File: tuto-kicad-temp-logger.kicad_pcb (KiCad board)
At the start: 4 copper layers, 60 x 45 mm, 68 parts, among them J201 HOOYA_USB_306F, J202 Conn_01x01_Pin, J401 SHOU HAN TF-CARD H1.8, Q301 L8050QLT1G, Q302 L8050QLT1G, SW301 TE_FSM4JSMATR, SW302 TE_FSM4JSMATR, U201 SGM2212-3.3XKC3G, U202 CP2102N-Axx-xQFN28, U301 ESP32-C3-WROOM-02, U401 TMP102xxDRL

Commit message: Routage
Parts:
- moved TP203 16.4 mm to (121.3, 99.1)
- moved TP204 12.1 mm to (120.5, 105.0)
- moved TP406 12.1 mm to (157.7, 91.5)
- moved TP205 9.83 mm to (134.3, 112.9)
- moved R402 7.32 mm to (126.2, 95.4), turned to 180 degrees
- moved TP401 7.24 mm to (123.0, 93.0)
- moved TP402 7.02 mm to (128.3, 91.2)
- moved TP403 5.50 mm to (133.1, 89.2)
- moved TP206 5.30 mm to (135.6, 106.8)
- moved TP301 5.00 mm to (111.9, 109.6)
- moved D201 4.80 mm to (156.5, 106.7)
- moved R403 4.50 mm to (144.8, 87.5), turned to -90 degrees
- moved TP303 4.24 mm to (109.0, 92.5)
- moved TP404 3.97 mm to (137.8, 86.8)
- moved TP407 2.91 mm to (149.3, 82.5)
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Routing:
- net /MCU/I2C.SDA: track 0.00 -> 65.8 mm, vias 0 -> 1
- net /MCU/I2C.SCL: track 0.00 -> 54.6 mm, vias 0 -> 1
- net GND: track 0.00 -> 54.6 mm, vias 0 -> 51
- net /MCU/SD.CD: track 0.00 -> 49.6 mm, vias 0 -> 1
- net /MCU/SD.SCK: track 0.00 -> 45.1 mm, vias 0 -> 1
- net /MCU/SD.MISO: track 0.00 -> 43.2 mm, vias 0 -> 1
- net /MCU/SD.CS: track 0.00 -> 38.8 mm, vias 0 -> 2
- net /MCU/SD.MOSI: track 0.00 -> 38.7 mm, vias 0 -> 1
- net /MCU/GPIO9: track 0.00 -> 37.1 mm, vias 0 -> 3
- net /MCU/UART.ESP32_TX: track 0.00 -> 35.3 mm, vias 0 -> 2
- net /MCU/UART.ESP32_RX: track 0.00 -> 33.8 mm, vias 0 -> 2
- net /MCU/CHIP_PU: track 0.00 -> 31.4 mm, vias 0 -> 1
- net VBUS: track 0.00 -> 26.8 mm, vias 0 -> 5
- net /MCU/RTS: track 0.00 -> 24.5 mm, vias 0 -> 4
- net +3V3: track 0.00 -> 22.6 mm, vias 0 -> 17
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- added copper zone on F.Cu, net +3V3
- added copper zone on In2.Cu, net +3V3
- added copper zone on In1.Cu, net GND
- added copper zone on In2.Cu, net VBUS
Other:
- board text added: "+3V3"
- board text added: "CD"
- board text added: "CHIP_PU"
- board text added: "CS"
- board text added: "DTR"
- board text added: "ESP32_RX"
- board text added: "ESP32_TX"
- board text added: "GND"
- board text added: "GPIO10"
- board text added: "GPIO18"
- board text added: "GPIO19"
- board text added: "GPIO9"
- board text added: "MISO"
- board text added: "MOSI"
- board text added: "RTS"
- board text added: "SCK"
- board text added: "SCL"
- board text added: "SDA"
- board text added: "VBUS"

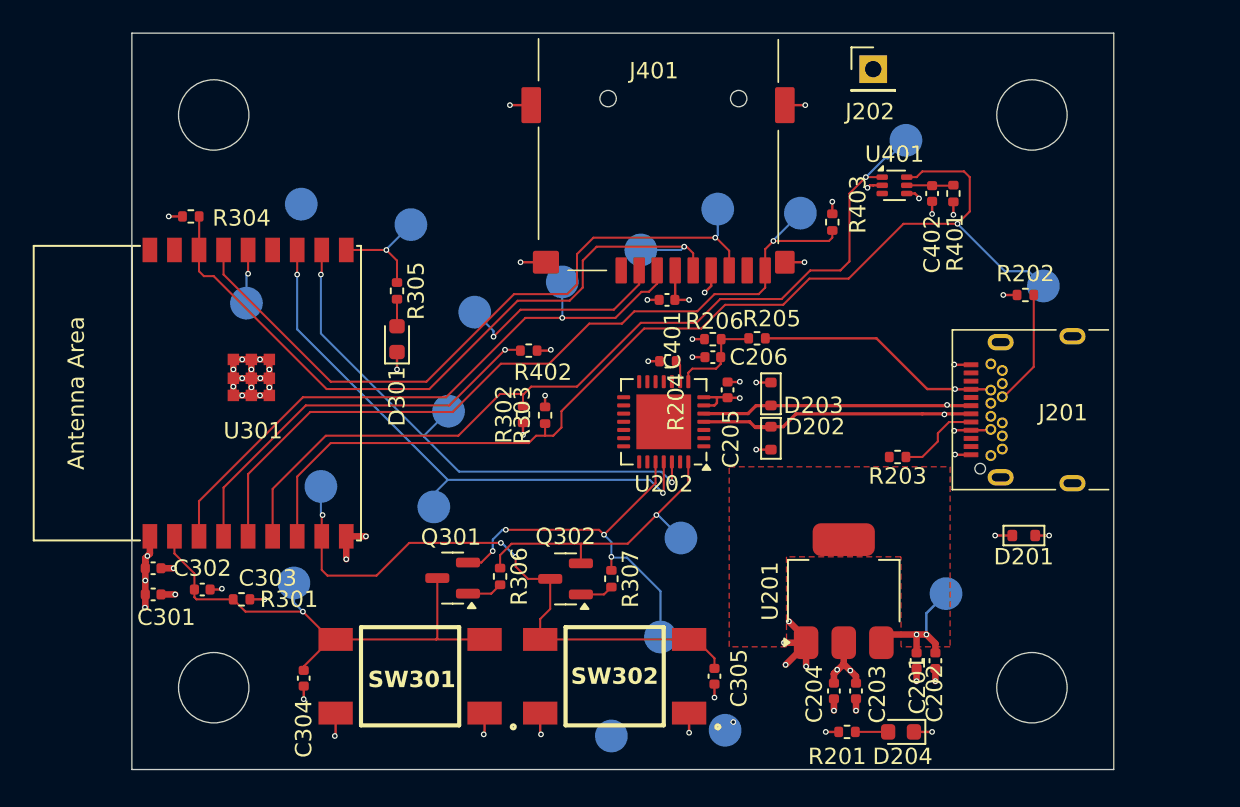
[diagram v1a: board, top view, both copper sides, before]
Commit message: Ajout de plans hachurés au top et bottom
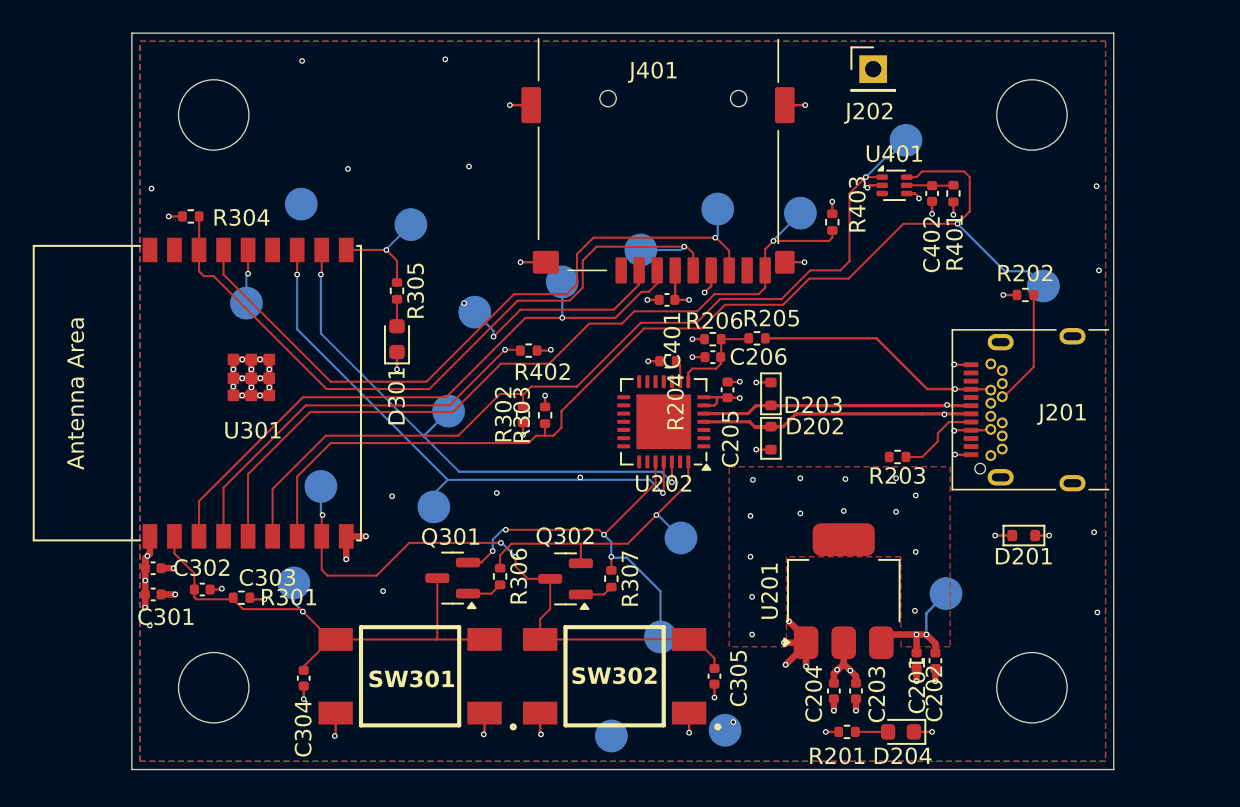
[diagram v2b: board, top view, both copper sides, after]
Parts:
- moved R301 0.10 mm to (108.7, 110.5)
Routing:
- net +3V3: track 22.6 -> 26.3 mm, vias 17 -> 31
- net GND: vias 51 -> 64
- net /MCU/UART.ESP32_TX: vias 2 -> 3
- net /MCU/SD.CS: vias 2 -> 3
- added copper zone on B.Cu, net GND
- added copper zone on F.Cu, net GND

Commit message: Ajout des annotations
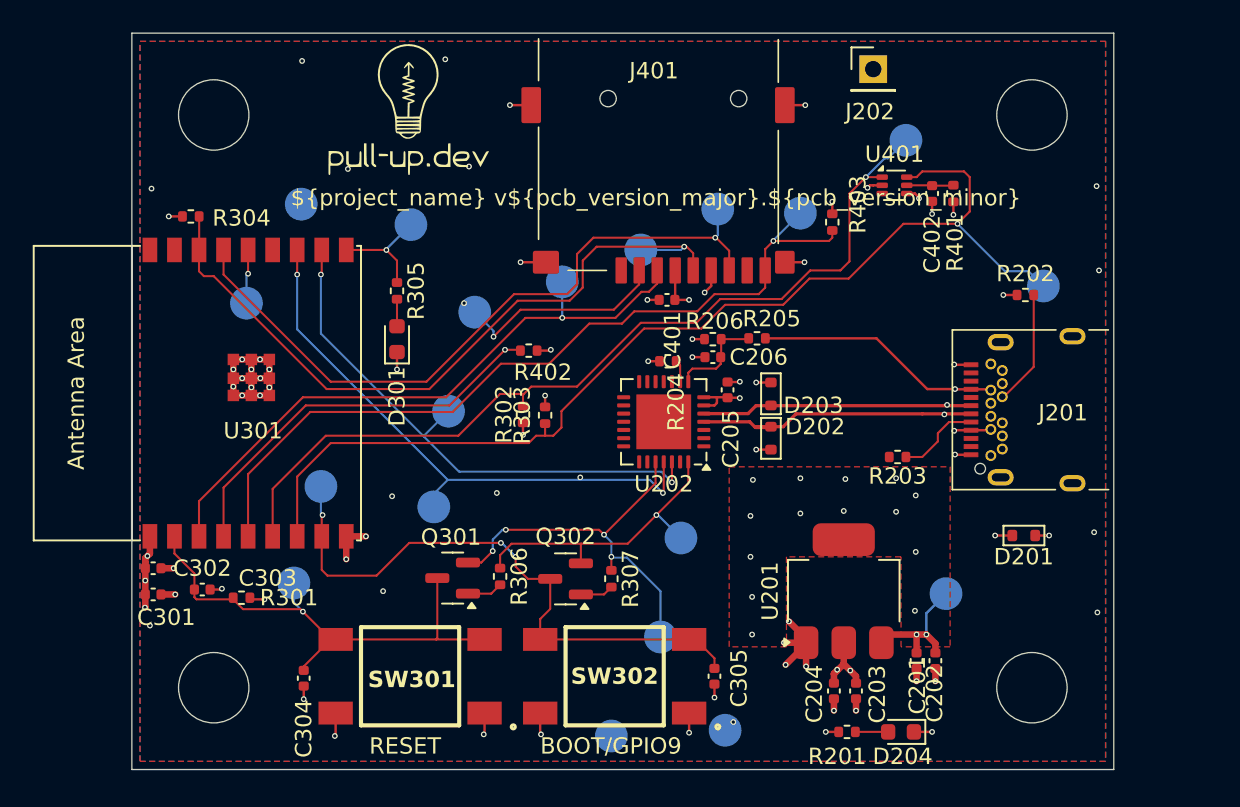
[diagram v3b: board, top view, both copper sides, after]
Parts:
- added G***: LOGO, tuto-kicad-temp-logger:logo, F.Cu at (118.9, 80.7)
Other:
- board text added: "${project_name} v${pcb_version_major}.${pcb_version_minor}"
- board text added: "BOOT/GPIO9"
- board text added: "RESET"

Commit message: Silkscreen, DRC et corrections
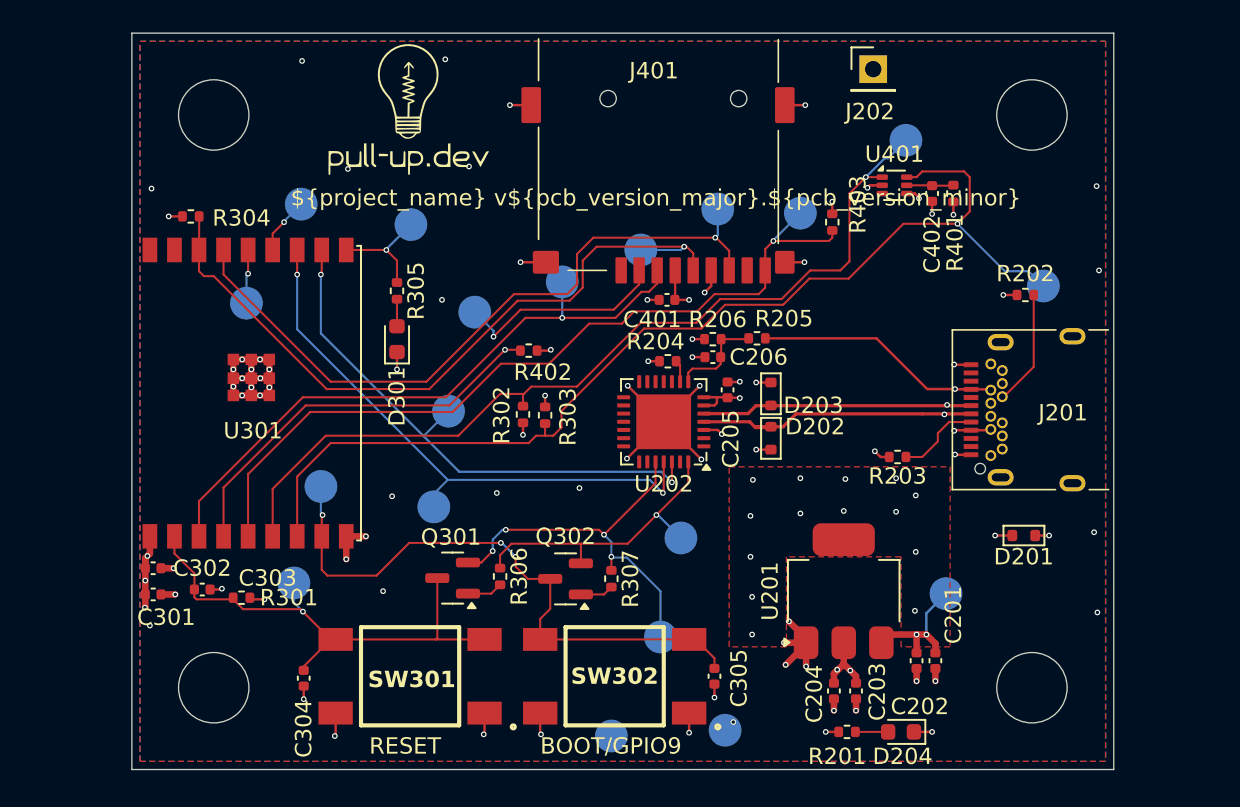
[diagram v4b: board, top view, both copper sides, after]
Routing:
- net GND: track 54.6 -> 69.5 mm, vias 64 -> 72
- net Net-(U301-GPIO18/USB_D-): track 0.00 -> 3.52 mm, vias 0 -> 1
- net /MCU/UART.ESP32_TX: vias 3 -> 2
- net /MCU/SD.CS: vias 3 -> 2
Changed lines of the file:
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@@
 		(tags "resistor")
 		(property "Reference" "R302"
-			(at 0 -1.17 -90)
+			(at -0.05 -1.3 -90)
 			(layer "F.SilkS")
 			(effects
@@
 		(tags "resistor")
 		(property "Reference" "R206"
-			(at -0.1 1.1 180)
+			(at -0.3 1.2 180)
 			(layer "F.SilkS")
 			(effects
@@
 		(tags "resistor")
 		(property "Reference" "R204"
-			(at 0.5 2.5 90)
+			(at -0.75 -1.2 180)
 			(layer "F.SilkS")
 			(effects
@@
 		(tags "resistor")
 		(property "Reference" "R303"
-			(at 0 1.4 90)
+			(at 0.1 -1.4 90)
 			(layer "F.SilkS")
 			(effects
@@
 		(tags "capacitor")
 		(property "Reference" "C401"
-			(at -0.3375 -2.475 -90)
+			(at 0.9 -1.2 0)
 			(layer "F.SilkS")
 			(effects
@@
 		(tags "resistor")
 		(property "Reference" "R205"
-			(at -0.9 1.2 180)
+			(at -1.65 1.2 180)
 			(layer "F.SilkS")
 			(effects
@@
 		(attr smd)
 		(fp_line
-			(start 9 -13)
-			(end 9 -6.5)
-			(stroke
-				(width 0.12)
-				(type solid)
-			)
-			(layer "F.SilkS")
-		)
-		(fp_line
-			(start -9 -13)
-			(end 9 -13)
-			(stroke
-				(width 0.12)
-				(type solid)
-			)
-			(layer "F.SilkS")
-		)
-		(fp_line
-			(start -9 -13)
-			(end -9 -6.5)
-			(stroke
-				(width 0.12)
-				(type solid)
-			)
-			(layer "F.SilkS")
-		)
-		(fp_line
-			(start 9 -7)
-			(end -8.95 -7)
-			(stroke
-				(width 0.12)
-				(type solid)
-			)
-			(layer "F.SilkS")
-		)
-		(fp_line
 			(start 9 6.75)
 			(end 9 7)
@@
 			(layer "F.Fab")
 		)
-		(fp_text user "Antenna Area"
-			(at 0 -10.4 -90)
-			(layer "F.SilkS")
-			(effects
-				(font
-					(size 1 1)
-					(thickness 0.15)
-				)
-			)
-		)
 		(fp_text user "${REFERENCE}"
 			(at 0 -1.75 -90)
@@
 		(tags "capacitor")
 		(property "Reference" "C202"
-			(at 2 -1.1 90)
+			(at 2.8 -0.2 180)
 			(layer "F.SilkS")
 			(effects
@@
 		(tags "capacitor")
 		(property "Reference" "C203"
-			(at 0.2 -1.3 90)
+			(at 0.05 -1.3 90)
 			(layer "F.SilkS")
 			(effects
@@
 		(tags "capacitor")
 		(property "Reference" "C201"
-			(at 1.5 1.1 90)
+			(at -2.8 -1.1 90)
 			(layer "F.SilkS")
 			(effects
@@
 	)
 	(segment
+		(start 134.5 99.75)
+		(end 132.25 102)
+		(width 0.15)
+		(layer "F.Cu")
+		(net 1)
+	)
+	(segment
 		(start 143.2 113)
 		(end 142.15 111.95)
@@
 	)
 	(segment
+		(start 134.5 99.75)
+		(end 136.7 97.55)
+		(width 0.15)
+		(layer "F.Cu")
+		(net 1)
+	)
+	(segment
 		(start 153.2775 96.265)
 		(end 152.265 96.265)
@@
 	)
 	(segment
+		(start 134.5 99.75)
+		(end 132.3 97.55)
+		(width 0.15)
+		(layer "F.Cu")
+		(net 1)
+	)
+	(segment
 		(start 137 91.85)
 		(end 137.4 91.45)
@@
 	)
 	(segment
+		(start 137.8 100.25)
+		(end 138.05 100.5)
+		(width 0.15)
+		(layer "F.Cu")
+		(net 1)
+	)
+	(segment
 		(start 151.1 114.83)
 		(end 151.1 115.6)
@@
 	)
 	(segment
+		(start 147.75 101.9)
+		(end 147.4 101.55)
+		(width 0.15)
+		(layer "F.Cu")
+		(net 1)
+	)
+	(segment
 		(start 147.3 85.3)
 		(end 147.1 85.3)
@@
 	)
 	(segment
+		(start 136.95 100.25)
+		(end 137.8 100.25)
+		(width 0.15)
+		(layer "F.Cu")
+		(net 1)
+	)
+	(segment
 		(start 143.2 113.35)
 		(end 141.95 114.6)
@@
 	)
 	(segment
+		(start 148.28 101.9)
+		(end 147.75 101.9)
+		(width 0.15)
+		(layer "F.Cu")
+		(net 1)
+	)
+	(segment
 		(start 143.2 113.25)
 		(end 141.85 113.25)
@@
 		(net 1)
 	)
+	(segment
+		(start 134.5 99.75)
+		(end 136.8 102.05)
+		(width 0.15)
+		(layer "F.Cu")
+		(net 1)
+	)
 	(via
 		(at 109.83 95.94)
@@
 	)
 	(via
+		(at 136.7 97.55)
+		(size 0.35)
+		(drill 0.2)
+		(layers "F.Cu" "B.Cu")
+		(net 1)
+	)
+	(via
 		(at 107.5 109.95)
 		(size 0.35)
@@
 	)
 	(via
+		(at 129.35 103.8)
+		(size 0.35)
+		(drill 0.2)
+		(layers "F.Cu" "B.Cu")
+		(net 1)
+	)
+	(via
 		(at 108.74 97.09)
 		(size 0.35)
@@
 	)
 	(via
+		(at 138.05 100.5)
+		(size 0.35)
+		(drill 0.2)
+		(layers "F.Cu" "B.Cu")
+		(net 1)
+	)
+	(via
 		(at 133.5 92.3)
 		(size 0.35)
@@
 	)
 	(via
+		(at 132.3 97.55)
+		(size 0.35)
+		(drill 0.2)
+		(layers "F.Cu" "B.Cu")
+		(net 1)
+	)
+	(via
 		(at 140.15 97.35)
 		(size 0.35)
@@
 	)
 	(via
+		(at 136.8 102.05)
+		(size 0.35)
+		(drill 0.2)
+		(layers "F.Cu" "B.Cu")
+		(net 1)
+	)
+	(via
 		(at 114.4 118.95)
 		(size 0.35)
@@
 	)
 	(via
+		(at 120.95 92.3)
+		(size 0.35)
+		(drill 0.2)
+		(layers "F.Cu" "B.Cu")
+		(net 1)
+	)
+	(via
 		(at 150.9 87.05)
 		(size 0.35)
@@
 	)
 	(via
+		(at 132.25 102)
+		(size 0.35)
+		(drill 0.2)
+		(layers "F.Cu" "B.Cu")
+		(net 1)
+	)
+	(via
 		(at 103.1 112.2)
 		(size 0.35)
@@
 		(net 1)
 	)
+	(via
+		(at 147.4 101.55)
+		(size 0.35)
+		(drill 0.2)
+		(layers "F.Cu" "B.Cu")
+		(net 1)
+	)
 	(segment
 		(start 151.1 113.87)
@@
 		(net 24)
 	)
-	(via
-		(at 122.3 92.5)
-		(size 0.35)
-		(drill 0.2)
-		(layers "F.Cu" "B.Cu")
-		(net 24)
-	)
 	(segment
 		(start 124.1 94.55)
@@
 		(net 40)
 	)
-	(via
-		(at 129.4 103.15)
-		(size 0.35)
-		(drill 0.2)
-		(layers "F.Cu" "B.Cu")
-		(net 40)
-	)
 	(segment
 		(start 134.45 104.1)
@@
 	)
 	(segment
+		(start 110.6 88.25)
+		(end 111.3 87.55)
+		(width 0.127)
+		(layer "F.Cu")
+		(net 41)
+	)
+	(segment
+		(start 110.6 89.25)
+		(end 110.6 88.25)
+		(width 0.127)
+		(layer "F.Cu")
+		(net 41)
+	)
+	(via
+		(at 111.3 87.55)
+		(size 0.35)
+		(drill 0.2)
+		(layers "F.Cu" "B.Cu")
+		(net 41)
+	)
+	(segment
+		(start 111.3 87.55)
+		(end 111.3 87.5)
+		(width 0.127)
+		(layer "B.Cu")
+		(net 41)
+	)
+	(segment
+		(start 111.3 87.5)
+		(end 112.35 86.45)
+		(width 0.127)
+		(layer "B.Cu")
+		(net 41)
+	)
+	(segment
